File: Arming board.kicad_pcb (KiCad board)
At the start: 2 copper layers, 46 parts, among them J2 Conn_01x01_Pin, J3 Conn_01x01_Pin, J4 Conn_01x04_Pin, Q1 SQS141ELNW-T1_GE3, Q2 SQS141ELNW-T1_GE3, U1 CD40107BE, U2 TSX3702ID, U3 TSX3702ID, U6 CD40107BE

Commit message: Add files via upload
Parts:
- removed J4: Conn_01x04_Pin, Connector_PinHeader_1.00mm:PinHeader_1x04_P1.00mm_Horizontal
- added J1: Conn_01x04_Pin, Connector_PinHeader_1.00mm:PinHeader_1x04_P1.00mm_Horizontal, F.Cu at (36.4, 101.5)
- moved J2 10.7 mm to (64.2, 107.2)
- moved J3 8.12 mm to (64.2, 109.4)
- moved C3 2.92 mm to (58.5, 83.5)
- moved C10 2.03 mm to (60.0, 111.4)
- moved F1 2.00 mm to (64.0, 90.5)
- moved C2 1.83 mm to (56.8, 92.0)
- moved R15 1.22 mm to (49.8, 119.2), turned to 180 degrees
- moved R18 1.03 mm to (57.0, 109.5)
- moved R16 1.01 mm to (57.0, 110.7)
- moved C8 0.96 mm to (56.5, 113.0)
- moved C9 0.96 mm to (56.5, 114.0)
- moved C6 0.90 mm to (44.6, 116.7)
- moved C1 0.87 mm to (44.8, 91.1)
- moved R4 0.83 mm to (57.8, 92.0)
- moved R5 0.80 mm to (50.2, 94.5)
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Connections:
- J2 pad 1: /Batt+ -> VCC
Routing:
- net GND: track 0.00 -> 155.2 mm, vias 0 -> 10
- net VCC: track 0.00 -> 134.4 mm, vias 0 -> 7
- net BATT_armed: track 0.00 -> 54.1 mm, vias 0 -> 7
- net /Arm_In_1: track 0.00 -> 46.4 mm, vias 0 -> 3
- net /Disarm_In_1: track 15.3 -> 59.1 mm, vias 0 -> 2
- net /Arming logic 1/out: track 0.00 -> 28.2 mm, vias 0 -> 1
- net /Arming logic 2/V+: track 0.00 -> 27.7 mm, vias 0 -> 2
- net /Arming logic 1/V+: track 0.00 -> 23.6 mm, vias 0 -> 1
- net Net-(D1-K): track 0.00 -> 20.3 mm, vias 0 -> 4
- net Net-(D3-K): track 0.00 -> 20.2 mm, vias 0 -> 2
- net /Arming logic 2/out: track 0.00 -> 19.5 mm, vias 0 -> 1
- net Net-(U1-A): track 0.00 -> 17.4 mm
- net Net-(U6-A): track 0.00 -> 16.3 mm
- net /Arming logic 1/-out: track 0.00 -> 15.8 mm
- net /Arming logic 2/-out: track 0.00 -> 14.8 mm
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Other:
- board outline added: 37.2 x 47.4 mm
- copper layers 2 -> 4

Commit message: continued scematic
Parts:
- moved J2 10.7 mm to (68.6, 97.5)
- moved J3 8.12 mm to (68.5, 102.5)
- moved C3 2.92 mm to (61.0, 85.0)
- moved R18 2.06 mm to (56.5, 107.5)
- moved C2 1.83 mm to (55.0, 91.6)
- moved F2 1.44 mm to (63.0, 116.5), turned to 0 degrees
- moved C10 1.00 mm to (61.0, 111.5)
- moved F1 1.00 mm to (63.0, 90.5), turned to 180 degrees
- moved C6 0.90 mm to (45.5, 116.7)
- moved C1 0.87 mm to (45.5, 91.6)
- moved R4 0.83 mm to (57.1, 91.6)
- moved C8 0.81 mm to (56.5, 112.2)
- moved C9 0.81 mm to (56.5, 113.2)
- moved R5 0.80 mm to (51.0, 94.5)
- moved R15 0.76 mm to (50.5, 119.5)
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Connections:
- J2 pad 1: VCC -> /Batt+
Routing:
- net VCC: track 134.4 -> 13.0 mm, vias 7 -> 0
- net GND: track 155.2 -> 39.5 mm, vias 10 -> 5
- net BATT_armed: track 54.1 -> 0.00 mm, vias 7 -> 0
- net /Disarm_In_1: track 59.1 -> 22.2 mm, vias 2 -> 0
- net /Arming logic 2/V+: track 27.7 -> 0.00 mm, vias 2 -> 0
- net /Arming logic 1/V+: track 23.6 -> 0.00 mm, vias 1 -> 0
- net /Arming logic 1/out: track 28.2 -> 6.24 mm, vias 1 -> 0
- net Net-(D1-K): track 20.3 -> 0.00 mm, vias 4 -> 0
- net /Arming logic 2/out: track 19.5 -> 0.00 mm, vias 1 -> 0
- net Net-(U6-A): track 16.3 -> 0.00 mm
- net /Arming logic 2/-out: track 14.8 -> 0.00 mm
- net Net-(D3-K): track 20.2 -> 7.59 mm, vias 2 -> 0
- net /Arming logic 1/-out: track 15.8 -> 25.5 mm
- net Net-(U6-E): track 9.63 -> 0.00 mm, vias 1 -> 0
- net Net-(U2B--): track 8.17 -> 0.00 mm
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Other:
- board outline removed

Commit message: continued schematic
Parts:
- removed C10, C3, C4, C5, C8, C9: 100n, Capacitor_SMD:C_0402_1005Metric
- removed C6, C7: 1u, Capacitor_SMD:C_0402_1005Metric
- removed DZ1, DZ2, DZ3: 16V, Diode_SMD:D_SOD-123
- removed F1, F2: 50m, Fuse:Fuse_Bourns_TBU-CA
- removed J3: Conn_01x01_Pin, Connector_PinHeader_1.00mm:PinHeader_1x01_P1.00mm_Horizontal
- removed Q1, Q2: SQS141ELNW-T1_GE3, eigene:POWERPAK-1212-8
- removed R11, R12, R13, R14, R15, R16, R17, R18, R2, R6, R7, R8: 10k, Resistor_SMD:R_0402_1005Metric
- removed U1, U6: CD40107BE, cd40107:DIP794W45P254L959H508Q8
- removed U2, U3: TSX3702ID, PCM_Package_SO_AKL:SO-8_3.9x4.9mm_P1.27mm
- added D5: ESD5Zxx, Diode_SMD:D_SOD-523, F.Cu at (65.8, 110.7)
- added IC1: CD4043BDR, rapid_arming:SOIC127P600X175-16N, F.Cu at (59.7, 110.3)
- C1, C2: value 1u -> C
- D1, D3: value 4.7 -> ESD5Zxx; footprint Diode_SMD:D_SOD-123 -> Diode_SMD:D_SOD-523
- J1: value Conn_01x04_Pin -> ~; footprint Connector_PinHeader_1.00mm:PinHeader_1x04_P1.00mm_Horizontal -> stigma:Molex_Micro-Fit_3.0_43045-0400_2x02_P3.00mm_Horizontal
- J2: value Conn_01x01_Pin -> ~; footprint Connector_PinHeader_1.00mm:PinHeader_1x01_P1.00mm_Horizontal -> stigma:Molex_Micro-Fit_3.0_43045-0400_2x02_P3.00mm_Horizontal
- R1, R5: footprint Resistor_SMD:R_0402_1005Metric -> Resistor_SMD:R_0402_1005Metric_Pad0.72x0.64mm_HandSolder
- R3, R4: value 10k -> R
- moved R1 39.5 mm to (76.5, 111.5), turned to 0 degrees
- moved R5 31.8 mm to (76.5, 113.5)
- moved C1 30.8 mm to (69.0, 111.5), turned to 0 degrees
- moved R4 27.3 mm to (73.4, 113.5), turned to 0 degrees
- moved R3 26.4 mm to (73.4, 111.5), turned to 0 degrees
- moved C2 25.9 mm to (69.0, 113.4), turned to 0 degrees
- moved R9 24.5 mm to (69.8, 106.0), turned to 0 degrees
- moved J1 23.3 mm to (60.1, 99.8), turned to 0 degrees
- moved D2 22.7 mm to (74.0, 109.2)
- moved R10 22.3 mm to (69.8, 109.0)
- moved D3 16.0 mm to (65.8, 108.2)
- moved D1 14.6 mm to (65.8, 105.8)
- moved D4 11.5 mm to (74.9, 106.2), turned to 0 degrees
- moved J2 4.32 mm to (72.3, 99.8)
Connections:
- C1 pad 1: Net-(U2A--) -> arm
- C2 pad 1: Net-(U2B--) -> disarm
- D4 pad 1: BATT_armed -> +BATT_ARM
- J1 pad 1: /Arm_In_1 -> GND
- J1 pad 3: GND -> +BATT
- J1 pad 4: /Disarm_In_1 -> +BATT
- J2 pad 1: /Batt+ -> GND
- R1 pad 1: /Arm_In_1 -> Net-(Q1-Pad4)
- R1 pad 2: Net-(U2A--) -> VCC
- R3 pad 1: /Disarm_In_1 -> Net-(D1-K)
- R3 pad 2: Net-(U2B--) -> arm
- R4 pad 1: Net-(U2B--) -> Net-(D3-K)
- R4 pad 2: GND -> disarm
- R5 pad 1: VCC -> Net-(IC1-ENABLE)
- R5 pad 2: Net-(D1-K) -> VCC
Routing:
- net /Arm_In_1: track 43.4 -> 0.00 mm, vias 2 -> 0
- net GND: track 39.5 -> 0.00 mm, vias 5 -> 0
- net /Arming logic 1/-out: track 25.5 -> 0.00 mm
- net /Disarm_In_1: track 22.2 -> 0.00 mm
- net Net-(U1-A): track 18.4 -> 0.00 mm
- net VCC: track 13.0 -> 0.00 mm
- net Net-(U1-E): track 10.8 -> 0.00 mm, vias 2 -> 0
- net Net-(D3-K): track 7.59 -> 0.00 mm
- net Net-(U3A--): track 6.52 -> 0.00 mm
- net /Arming logic 1/out: track 6.24 -> 0.00 mm
- net Net-(U2A--): track 6.21 -> 0.00 mm
- net Net-(R10-Pad1): track 1.76 -> 0.00 mm

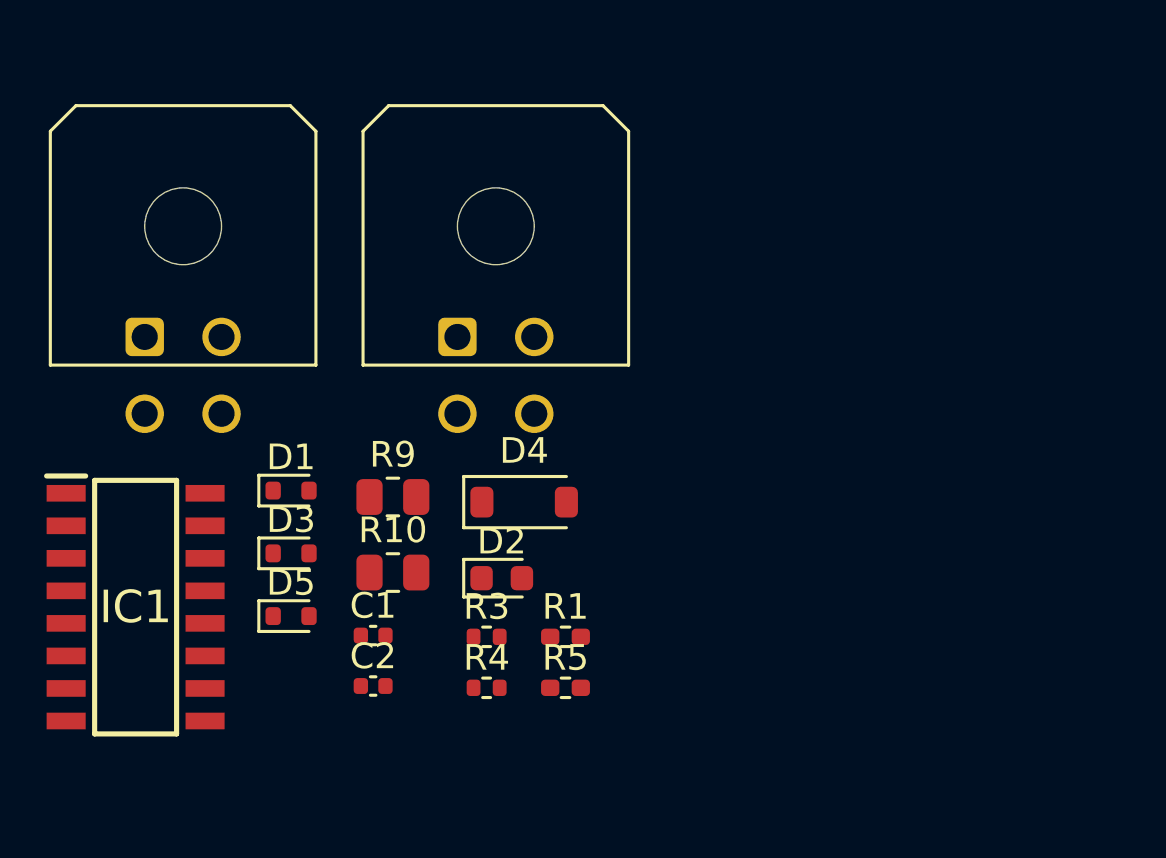
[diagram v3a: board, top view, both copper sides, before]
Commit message: finished first scematic draft
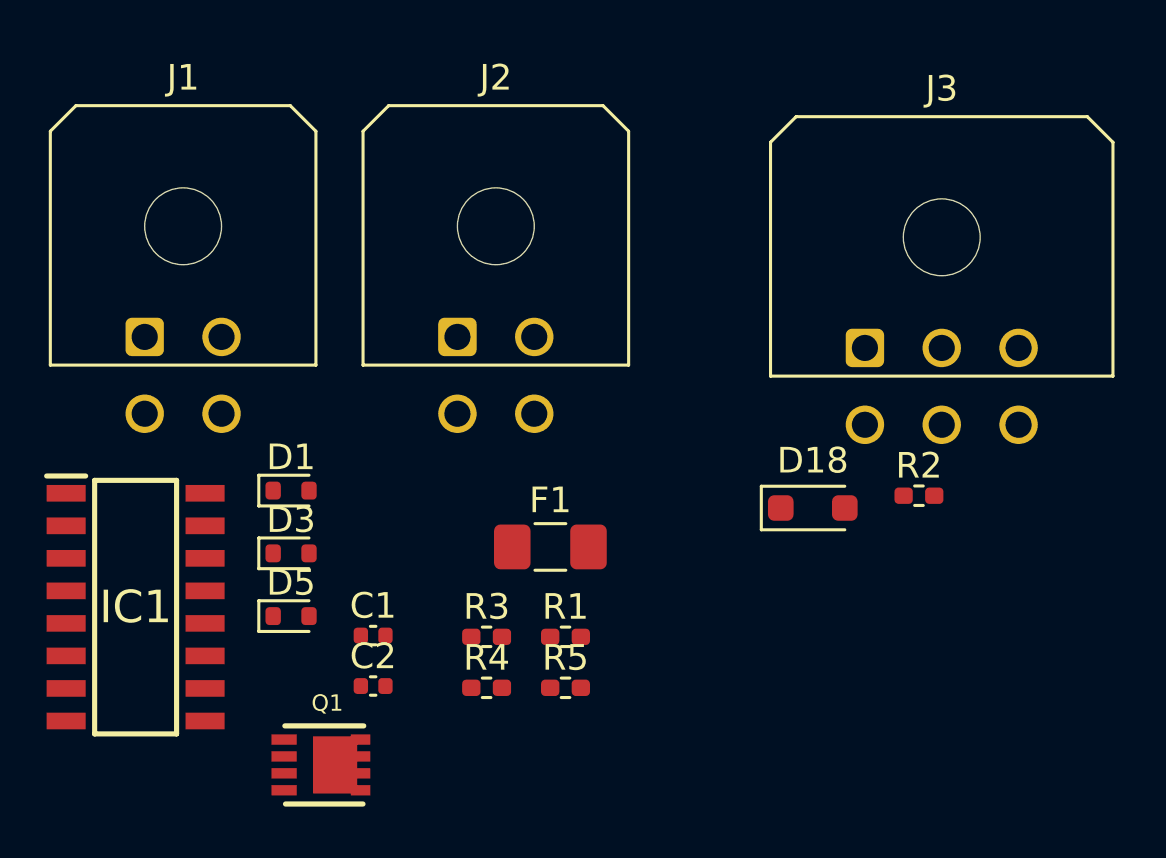
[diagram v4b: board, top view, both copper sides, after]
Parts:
- removed D2: LED, LED_SMD:LED_0603_1608Metric
- removed D4: 16V, Diode_SMD:D_SOD-123
- removed R10, R9: 4.7k, Resistor_SMD:R_0805_2012Metric
- added D18: D, Diode_SMD:D_SOD-323_HandSoldering, F.Cu at (86.2, 106.5)
- added F1: 200mA, Fuse:Fuse_1206_3216Metric_Pad1.42x1.75mm_HandSolder, F.Cu at (75.9, 108.0)
- added J3: Conn_02x03_Counter_Clockwise, Connector_Molex:Molex_Micro-Fit_3.0_43045-0600_2x03_P3.00mm_Horizontal, F.Cu at (88.2, 100.2)
- added Q1: SQS141ELNW-T1_GE3, rapid_arming:POWERPAK-1212-8, F.Cu at (67.1, 116.5)
- added R2: 1k, Resistor_SMD:R_0402_1005Metric_Pad0.72x0.64mm_HandSolder, F.Cu at (90.3, 106.0)
- C1, C2: value C -> 1u
- D5: value ESD5Zxx -> TS1811LD-CX
- J1, J2: footprint stigma:Molex_Micro-Fit_3.0_43045-0400_2x02_P3.00mm_Horizontal -> Connector_Molex:Molex_Micro-Fit_3.0_43045-0400_2x02_P3.00mm_Horizontal
- R3, R4: value R -> 10k; footprint Resistor_SMD:R_0402_1005Metric -> Resistor_SMD:R_0402_1005Metric_Pad0.72x0.64mm_HandSolder
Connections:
- R3 pad 1: Net-(D1-K) -> arm
- R3 pad 2: arm -> Net-(D1-K)
- R4 pad 1: Net-(D3-K) -> disarm
- R4 pad 2: disarm -> Net-(D3-K)

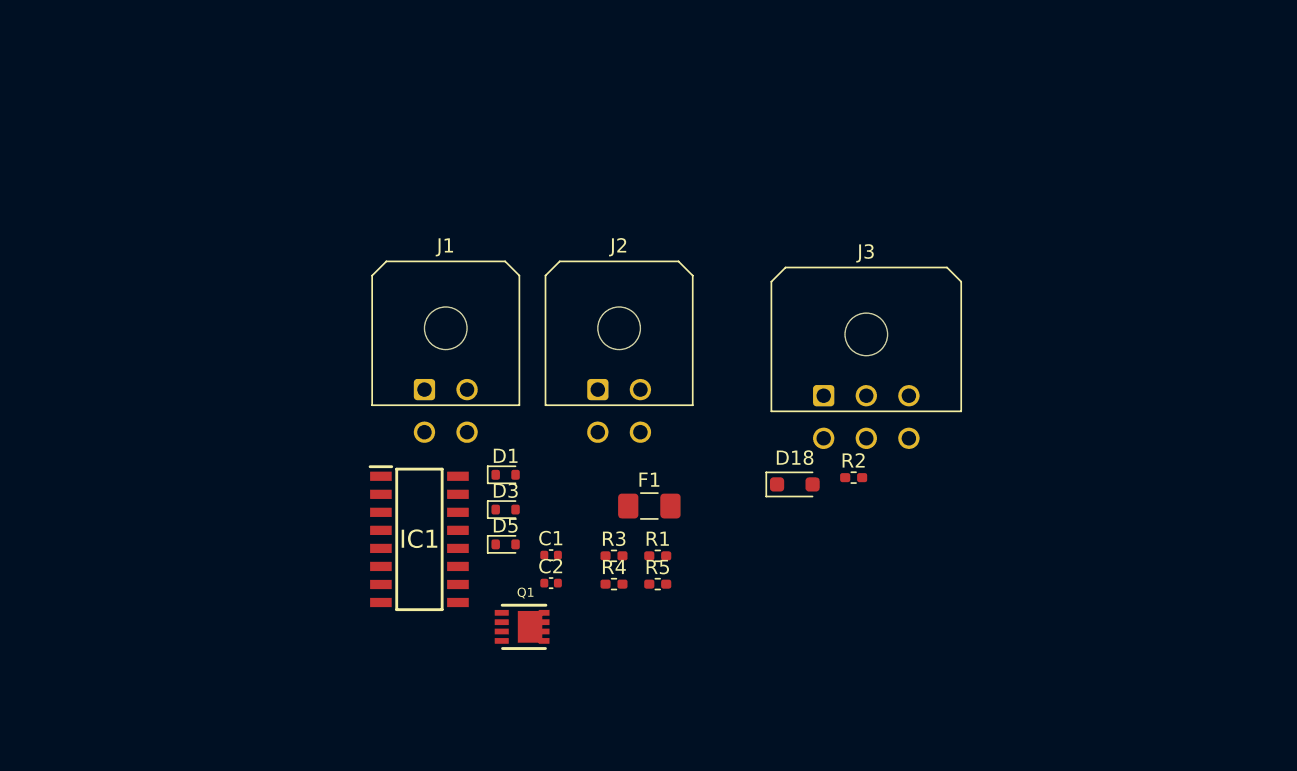
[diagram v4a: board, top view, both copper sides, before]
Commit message: Replaced connector with molex, fixed mosfet footprint
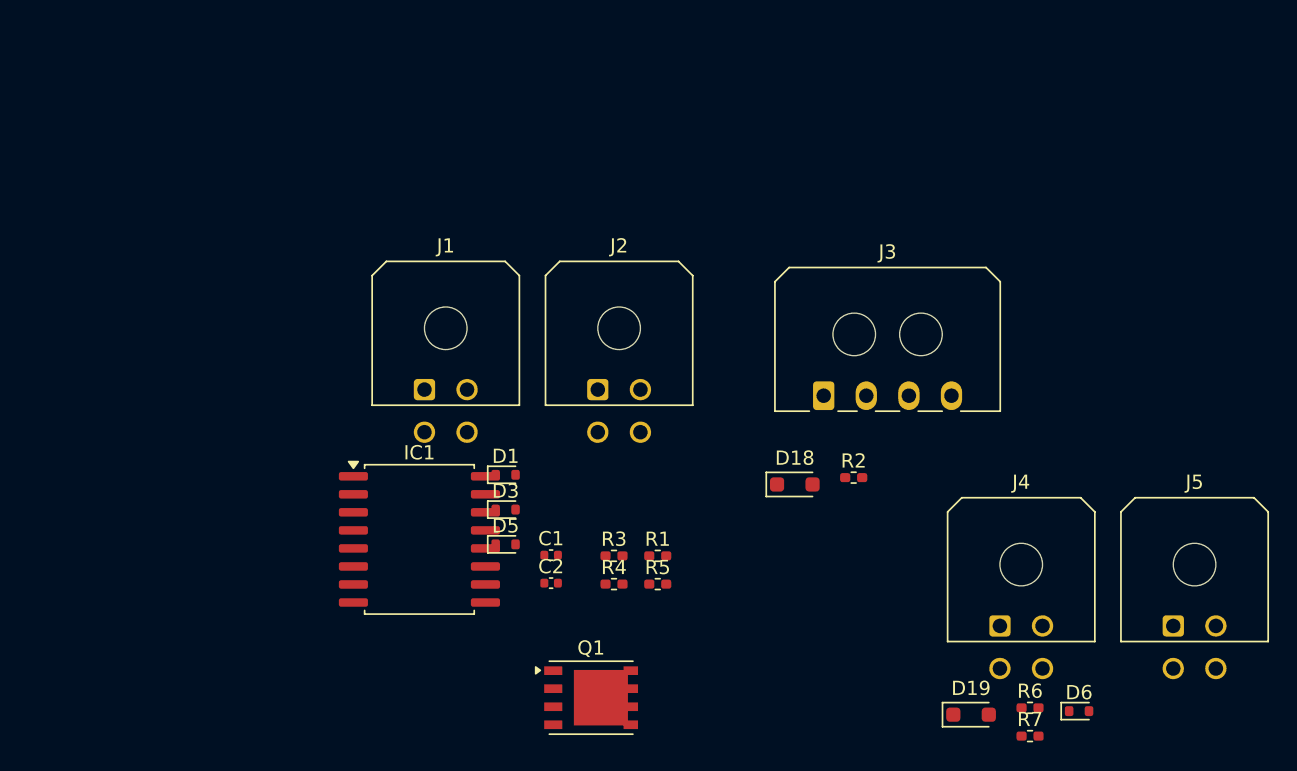
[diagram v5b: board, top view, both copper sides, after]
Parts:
- removed F1: 200mA, Fuse:Fuse_1206_3216Metric_Pad1.42x1.75mm_HandSolder
- added D19: D, Diode_SMD:D_SOD-323_HandSoldering, F.Cu at (98.6, 122.7)
- added D6: TS1811LD-CX, Diode_SMD:D_SOD-523, F.Cu at (106.2, 122.4)
- added J4: ~, Connector_Molex:Molex_Micro-Fit_3.0_43045-0400_2x02_P3.00mm_Horizontal, F.Cu at (100.6, 116.4)
- added J5: ~, Connector_Molex:Molex_Micro-Fit_3.0_43045-0400_2x02_P3.00mm_Horizontal, F.Cu at (112.8, 116.4)
- added R6: 10k, Resistor_SMD:R_0402_1005Metric_Pad0.72x0.64mm_HandSolder, F.Cu at (102.7, 122.2)
- added R7: 10k, Resistor_SMD:R_0402_1005Metric_Pad0.72x0.64mm_HandSolder, F.Cu at (102.7, 124.2)
- IC1: footprint rapid_arming:SOIC127P600X175-16N -> Package_SO:SOIC-16W_7.5x10.3mm_P1.27mm
- J3: value Conn_02x03_Counter_Clockwise -> Conn_01x04; footprint Connector_Molex:Molex_Micro-Fit_3.0_43045-0600_2x03_P3.00mm_Horizontal -> Connector_Molex:Molex_Micro-Fit_3.0_43650-0400_1x04_P3.00mm_Horizontal
- Q1: footprint rapid_arming:POWERPAK-1212-8 -> Package_SO:PowerPAK_SO-8_Single
- moved Q1 6.88 mm to (71.8, 121.5)
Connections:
- J3 pad 2: GND -> Net-(D3-K)
- J3 pad 3: sig_armed -> Net-(D1-K)
- J3 pad 4: Net-(D3-K) -> VCC
